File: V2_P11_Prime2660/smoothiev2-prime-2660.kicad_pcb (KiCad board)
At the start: 4 copper layers, 110 x 110 mm, 427 parts, among them J1 USB_B, J10 Conn_01x02, J11 Conn_01x02, J12 Conn_01x02, J13 Conn_01x02, J14 Conn_01x02, J15 Conn_01x02, J16 Conn_01x02, J17 Conn_01x02, J18 Conn_01x02, J19 Conn_01x02, J2 USB_A, J20 Conn_01x02, J21 Conn_01x02, J22 Conn_01x02, J23 Conn_01x02, J24 Conn_01x03, J25 Conn_01x03, J26 Conn_01x03, J27 Conn_01x03, J28 Conn_01x03, J29 Conn_01x03, J3 Micro_SD_Card_Det, J30 Conn_01x03_Male, J31 Conn_01x04, J32 Conn_02x05_Odd_Even, J33 Conn_02x05_Odd_Even, J34 Conn_02x05_Odd_Even, J35 Conn_02x05_Odd_Even, J36 Conn_02x05_Odd_Even, J37 Conn_02x05_Odd_Even, J38 Conn_02x05_Odd_Even, J39 Conn_02x05_Odd_Even, J4 RJ45_Hanrun_HR911105A, J40 Conn_02x05_Odd_Even, J41 Conn_ARM_JTAG_SWD_10, J42 Conn_01x02, J43 Conn_01x02, J44 Conn_01x02, J45 Conn_01x02, J5 Screw_Terminal_01x04, J6 Screw_Terminal_01x04, J7 Screw_Terminal_01x04, J8 Screw_Terminal_01x04, J9 Conn_01x02, Q17 WSD3066DN33, Q18 WSD3066DN33, Q19 WSD3066DN33, Q20 WSD3066DN33, Q21 WSD3066DN33, Q22 WSD3066DN33, Q23 CJ2301 S1, Q24 CJ2301 S1, Q25 WSD30L40DN, Q26 2N7002, Q27 MBT3906DW1, Q28 SQ3493EV, Q29 MBT3906DW1, Q30 SQ3493EV, Q31 MBT3906DW1, Q32 SQ3493EV, SW1 SW_Push, SW2 TS-1185EC-C-D-B, U1 LAN8720A, U10 TPD4E1U06DCKR, U11 TPD4E1U06DCKR, U12 LMV324, U13 TPD4E1U06DCKR, U14 TPD4E1U06DCKR, U15 74LCX07, U16 MT9700, U17 TPD4E1U06DCKR, U18 MT9700, U19 MT9700, U2 STM32H745XIHx, U20 MT9700, U21 TPS5430DDA, U22 MT3410L, U23 AP22814AW5, U24 LMV331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

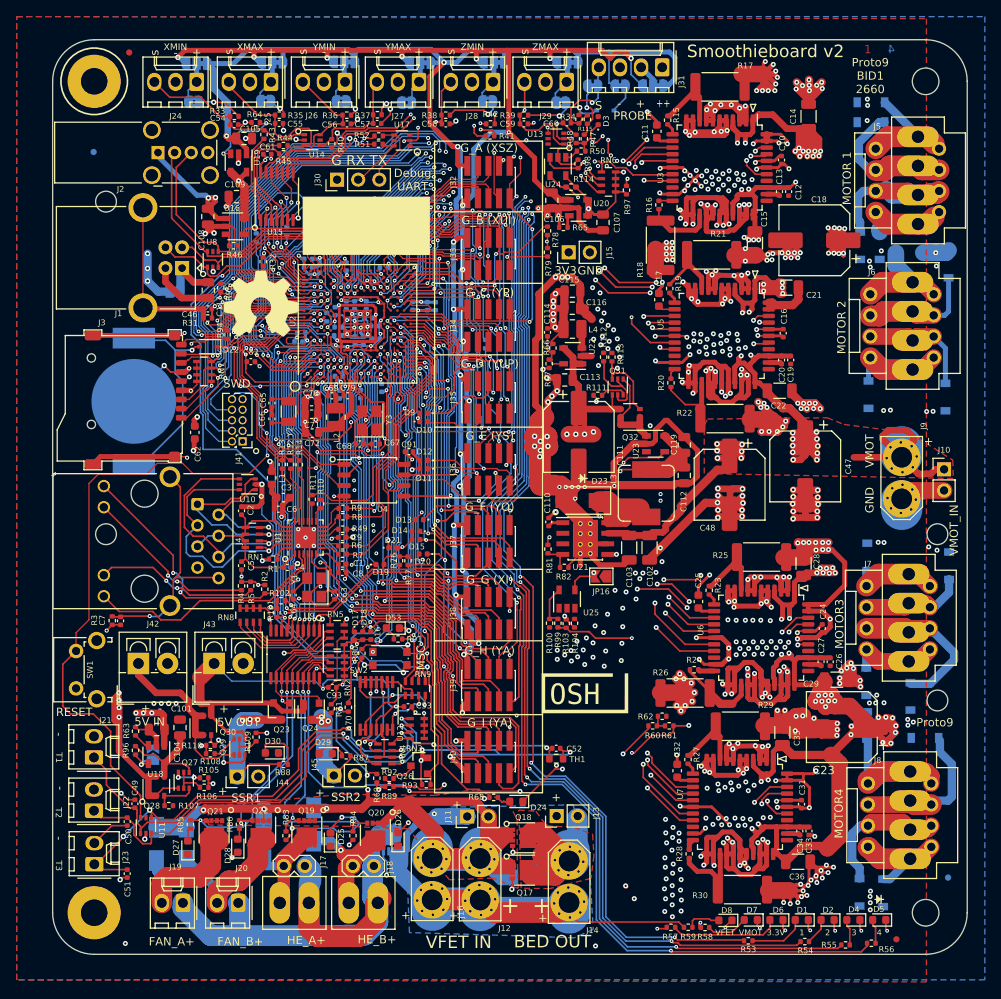
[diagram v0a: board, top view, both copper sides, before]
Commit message: Added 3d models, renders and stepfiles
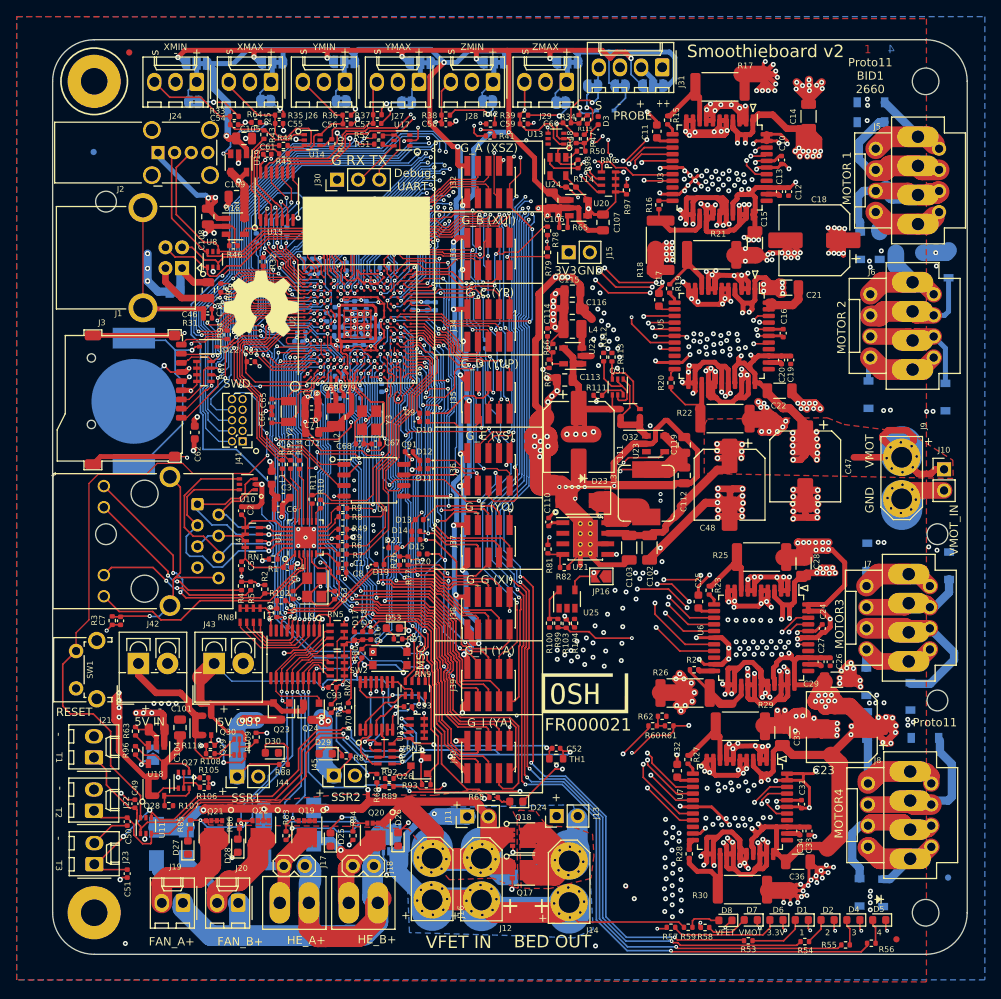
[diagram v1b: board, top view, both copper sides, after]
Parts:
- moved LOGO1 9.64 mm to (145.5, 88.5)
- moved LOGO3 1.26 mm to (162.7, 50.9)
- moved J12 0.15 mm to (151.4, 139.0)
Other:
- board text added: "6x Endstop connectors supporting Min and Max stops for X, Y, and Z"
- board text added: "ANALOG -3x buffered thermistor inputs -PCB thermistor -Motor power sense -Vfet power sense"
- board text added: "Comparator buffered probe input allows Trigger voltages from 3-45v (Ranges switched by jumpers)"
- board text added: "Controlled MOSFETs 4x Low side switching FET with High Side shutoff FET 2 for fan 2 for hotends"
- board text added: "Developed in multiple open source communities based on the feedback from our users and developers. Thanks to all who give back to open source. Extra special thanks to: Kliment and Wolfmanjm"
- board text added: "FR000021"
- board text added: "Proto11"
- board text added: "Proto11 BID1 2660"
- board text added: "USB MASTER USB-A connector (currently not functional in firmware)"
- board text added: "https://github.com/Smoothieware/SmoothieV2/wiki"
- board text removed: "7x Endstop connectors supporting Min and Max stops for X, Y, and Z plus a Probe"
- board text removed: "ANALOG 3x thermistor inputs board thermistor primary power sense vfet power sense dac"
- board text removed: "Controlled MOSFETs 4x High side controlled mosfets 2 for fan 2 for hotends"
- board text removed: "Proto9"
- board text removed: "Proto9 BID1 2660"
- board text removed: "USB MASTER USB-A connector supporting mass storage devices"
